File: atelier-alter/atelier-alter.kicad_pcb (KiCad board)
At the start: 2 copper layers, 81.8 x 80.2 mm, 59 parts, among them SW1 RESET, SW2 SW_DPST, SW3 SW_DPST, SW4 SW_DPST, U1 ATmega32U4-A, U2 PRTR5V0U2X, Y1 16Mhz

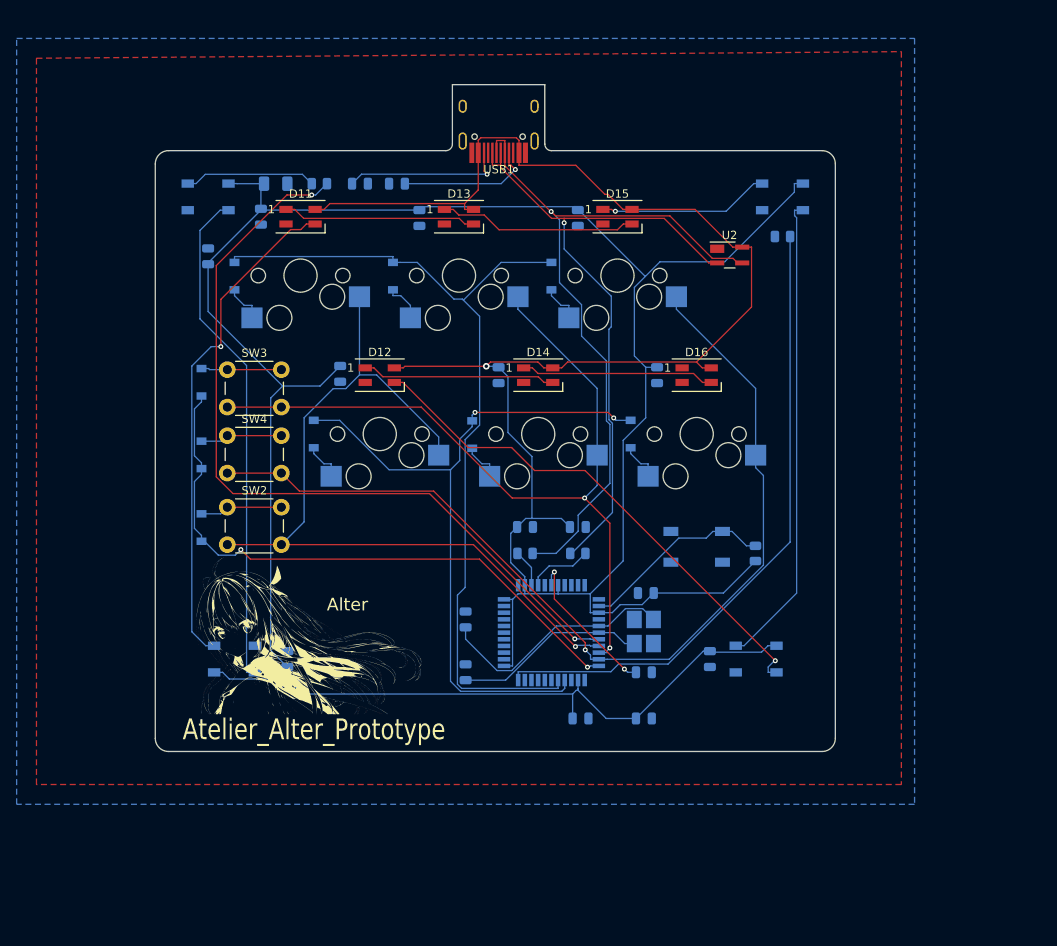
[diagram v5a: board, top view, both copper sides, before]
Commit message: update footprint, route lai mach, giam manh so luong vias
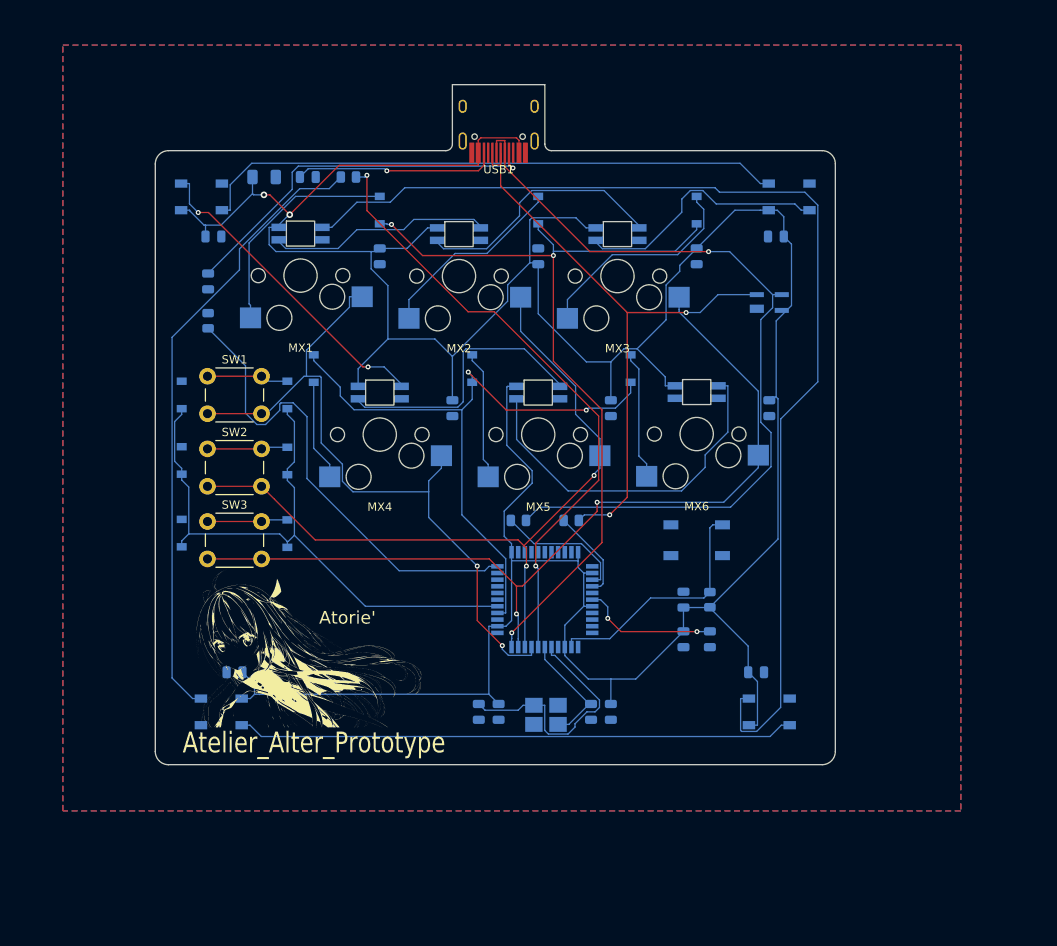
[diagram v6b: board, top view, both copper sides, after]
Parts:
- removed D1, D3, D4, D6: SOD-123, Diode_SMD:D_SOD-123
- removed D10, D7, D8: SK6812, LED_SMD:LED_SK6812_PLCC4_5.0x5.0mm_P3.2mm
- removed D14, D15, D16: SK6812MINI, LED_SMD:LED_SK6812MINI_PLCC4_3.5x3.5mm_P1.75mm
- added D21: SOD-123, Diode_SMD:D_SOD-123, B.Cu at (128.6, 84.9)
- added D22: SOD-123, Diode_SMD:D_SOD-123, B.Cu at (147.6, 84.9)
- added D23: SOD-123, Diode_SMD:D_SOD-123, B.Cu at (166.7, 84.9)
- added D31: SOD-123, Diode_SMD:D_SOD-123, B.Cu at (125.4, 88.1)
- added D32: SOD-123, Diode_SMD:D_SOD-123, B.Cu at (125.4, 96.0)
- added D33: SOD-123, Diode_SMD:D_SOD-123, B.Cu at (125.4, 104.8)
- added DT11: SK6812, LED_SMD:LED_SK6812_PLCC4_5.0x5.0mm_P3.2mm, B.Cu at (115.1, 64.3)
- C14, C17: value 100uF -> 100nF
- C2: value 1uF -> 22pF
- C4: value 22pF -> 0.1uF
- C6: value 0.1uF -> 1uF
- C8, C9: value 100nF -> 100uF
- D11, D12, D13: value SK6812MINI -> SOD-123; footprint LED_SMD:LED_SK6812MINI_PLCC4_3.5x3.5mm_P1.75mm -> Diode_SMD:D_SOD-123; moved to B.Cu
- D2, D5: value SOD-123 -> SK6812; footprint Diode_SMD:D_SOD-123 -> LED_SMD:LED_SK6812_PLCC4_5.0x5.0mm_P3.2mm
- MX1, MX2, MX3, MX4, MX5, MX6: value MX-NoLED -> Cherry_MX_Cherry_MX_RGB; footprint MX_Only:MXOnly-1U-Hotswap -> Cherry MX:Cherry-MX_PCB-Mounted_LTST-A683CEGBW_Kailh_Socket
- R4: value 10k -> 5.1k; footprint Resistor_SMD:R_0805_2012Metric -> Capacitor_SMD:C_0805_2012Metric
- R5: value 300 -> 5.1k; footprint Resistor_SMD:R_0805_2012Metric -> Capacitor_SMD:C_0805_2012Metric
- R6: value 5.1k -> 10k; footprint Capacitor_SMD:C_0805_2012Metric -> Resistor_SMD:R_0805_2012Metric
- R7: value 5.1k -> 300; footprint Capacitor_SMD:C_0805_2012Metric -> Resistor_SMD:R_0805_2012Metric
- SW1: value RESET -> SW_DPST; footprint random-keyboard-parts:SKQG-1155865 -> Button_Switch_THT:SW_PUSH_6mm_H9.5mm; moved to F.Cu
- SW4: value SW_DPST -> RESET; footprint Button_Switch_THT:SW_PUSH_6mm_H9.5mm -> random-keyboard-parts:SKQG-1155865; moved to B.Cu
- U2: moved to B.Cu
- moved R4 69.3 mm to (115.9, 74.5), turned to 90 degrees
- moved SW1 62.3 mm to (115.8, 85.9), turned to 0 degrees
- moved D5 58.6 mm to (183.4, 126.2), turned to 0 degrees
- moved SW4 57.8 mm to (174.6, 105.6), turned to 180 degrees
- moved C17 55.9 mm to (116.5, 69.1), turned to 0 degrees
- moved C9 49.7 mm to (136.5, 71.4)
- moved C10 49.5 mm to (119.1, 121.4), turned to 180 degrees
- moved C12 48.0 mm to (164.3, 89.7)
- moved C14 42.9 mm to (184.2, 69.1), turned to 180 degrees
- moved D2 35.2 mm to (117.5, 126.2), turned to 180 degrees
- moved C8 34.6 mm to (145.3, 89.7)
- moved C15 32.8 mm to (183.4, 89.7)
- moved D13 28.6 mm to (174.6, 65.9), turned to 90 degrees
- moved R6 28.1 mm to (115.9, 79.2), turned to 90 degrees
- moved C13 27.7 mm to (155.6, 71.4), turned to -90 degrees
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- renumbered Alter to Atorie'
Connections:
- C14 pad 1: GND -> +5V
- C14 pad 2: +5V -> GND
- C17 pad 1: GND -> +5V
- C17 pad 2: +5V -> GND
- C4 pad 1: GND -> +5V
- C4 pad 2: Net-(C4-Pad2) -> GND
- C6 pad 1: +5V -> GND
- C6 pad 2: GND -> Net-(C6-Pad2)
- C8 pad 1: +5V -> GND
- C8 pad 2: GND -> +5V
- C9 pad 1: +5V -> GND
- C9 pad 2: GND -> +5V
- D11 pad 1: Net-(D11-Pad1) -> ROW1
- D11 pad 2: GND -> Net-(D11-Pad2)
- D12 pad 1: Net-(D12-Pad1) -> ROW1
- D12 pad 2: GND -> Net-(D12-Pad2)
- D13 pad 1: Net-(D13-Pad1) -> ROW1
- D13 pad 2: GND -> Net-(D13-Pad2)
- D2 pad 1: ROW2 -> GND
- D5 pad 1: ROW1 -> GND
- D5 pad 2: Net-(D5-Pad2) -> Net-(D2-Pad4)
- MX1 pad 1: COL1 -> GND
- MX1 pad 2: Net-(D1-Pad2) -> D11
- MX2 pad 1: COL1 -> GND
- MX2 pad 2: Net-(D2-Pad2) -> Net-(MX1-Pad3)
- MX3 pad 1: COL2 -> GND
- MX3 pad 2: Net-(D3-Pad2) -> Net-(MX2-Pad3)
- MX4 pad 1: COL2 -> GND
- MX4 pad 2: Net-(D4-Pad2) -> D21
- MX5 pad 1: COL3 -> GND
- MX5 pad 2: Net-(D5-Pad2) -> Net-(MX4-Pad3)
- MX6 pad 1: COL3 -> GND
- MX6 pad 2: Net-(D6-Pad2) -> Net-(MX5-Pad3)
- R4 pad 1: Net-(R4-Pad1) -> GND
- R4 pad 2: GND -> Net-(R4-Pad2)
- R5 pad 1: RGB -> GND
- R5 pad 2: Net-(D7-Pad2) -> Net-(R5-Pad2)
- R6 pad 1: GND -> Net-(R6-Pad1)
- R6 pad 2: Net-(R6-Pad2) -> GND
- R7 pad 1: GND -> RGB
- R7 pad 2: Net-(R7-Pad2) -> Net-(D2-Pad2)
- SW1 pad 1: GND -> Net-(D31-Pad2)
- SW1 pad 2: Net-(R3-Pad1) -> COL1
- SW2 pad 1: Net-(D17-Pad2) -> Net-(D32-Pad2)
- SW2 pad 2: COL1 -> COL2
- SW3 pad 1: Net-(D18-Pad2) -> Net-(D33-Pad2)
- SW3 pad 2: COL2 -> COL3
- SW4 pad 1: Net-(D19-Pad2) -> GND
- SW4 pad 2: COL3 -> Net-(R3-Pad1)
- U1 pad 16: Net-(C4-Pad2) -> Net-(C3-Pad2)
- U1 pad 17: Net-(C3-Pad2) -> Net-(C2-Pad2)
- U1 pad 22: ROW3 -> ROW1
- U1 pad 27: ROW1 -> ROW3
- U1 pad 33: Net-(R4-Pad1) -> Net-(R6-Pad1)
- U1 pad 6: Net-(C2-Pad2) -> Net-(C6-Pad2)
- USB1 pad 10: Net-(R7-Pad2) -> Net-(R5-Pad2)
- USB1 pad 4: Net-(R6-Pad2) -> Net-(R4-Pad2)
- Y1 pad 1: Net-(C4-Pad2) -> Net-(C3-Pad2)
- Y1 pad 3: Net-(C3-Pad2) -> Net-(C2-Pad2)
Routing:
- net +5V: track 482.4 -> 403.9 mm, vias 1 -> 2
- net Net-(R4-Pad1): track 76.9 -> 0.00 mm
- net D11: track 60.5 -> 135.6 mm, vias 1 -> 0
- net Net-(D2-Pad2): track 4.81 -> 75.2 mm
- net Net-(D2-Pad4): track 0.00 -> 67.0 mm
- net Net-(D7-Pad4): track 60.9 -> 0.00 mm
- net Net-(R6-Pad1): track 0.00 -> 57.4 mm
- net Net-(R4-Pad2): track 0.00 -> 45.4 mm, vias 0 -> 1
- net Net-(MX5-Pad3): track 0.00 -> 43.4 mm
- net Net-(MX4-Pad3): track 0.00 -> 33.3 mm
- net Net-(MX2-Pad3): track 0.00 -> 30.7 mm
- net Net-(C4-Pad2): track 29.2 -> 0.00 mm
- net Net-(D11-Pad2): track 0.00 -> 27.1 mm
- net Net-(MX1-Pad3): track 0.00 -> 26.8 mm
- net Net-(D13-Pad2): track 0.00 -> 26.4 mm
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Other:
- board size 81.8 x 80.2 mm -> 81.8 x 81.8 mm

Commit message: add M2 mounting hole
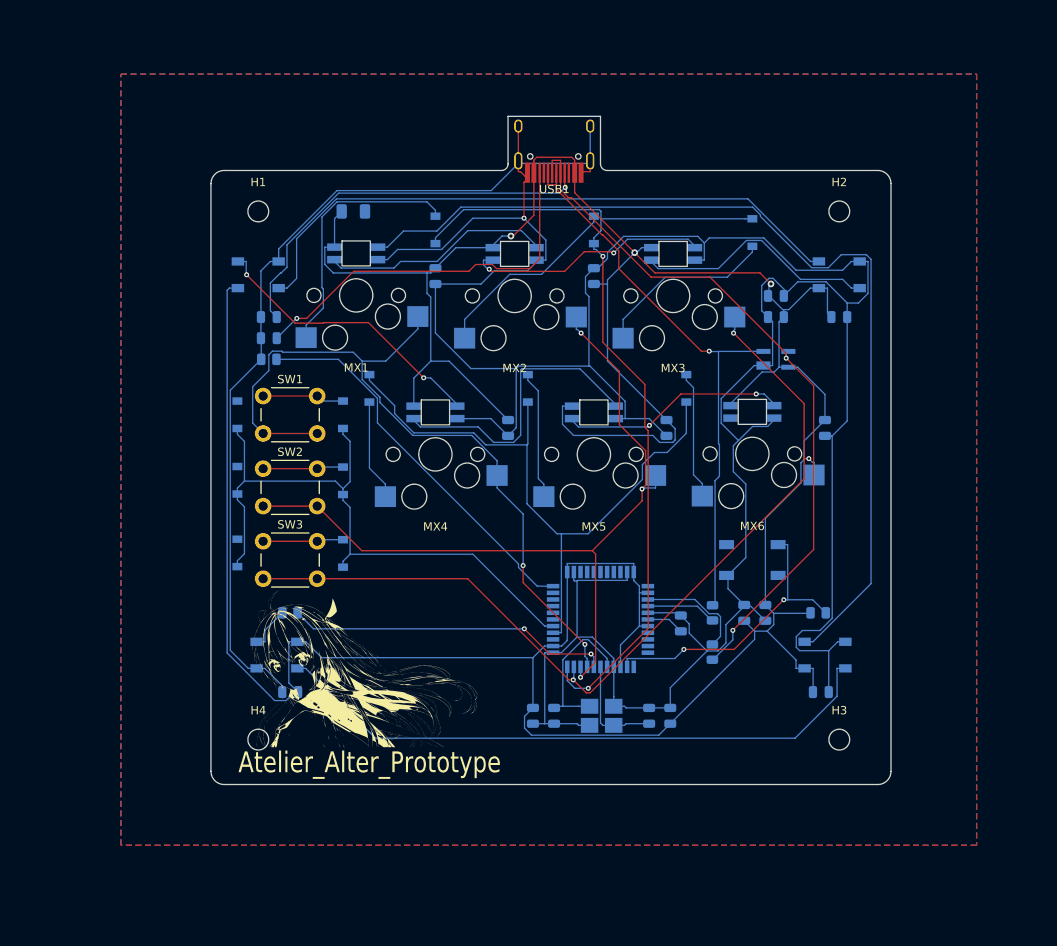
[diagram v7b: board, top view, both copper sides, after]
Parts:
- added H1: MountingHole, MountingHole:MountingHole_2.5mm, F.Cu at (121.9, 66.0)
- added H2: MountingHole, MountingHole:MountingHole_2.5mm, F.Cu at (191.8, 66.0)
- added H3: MountingHole, MountingHole:MountingHole_2.5mm, F.Cu at (191.8, 129.5)
- added H4: MountingHole, MountingHole:MountingHole_2.5mm, F.Cu at (121.9, 129.5)
- moved C17 75.9 mm to (191.8, 78.7)
- moved R7 52.9 mm to (125.7, 114.3)
- moved R1 28.2 mm to (176.5, 119.0), turned to 90 degrees
- moved C1 20.6 mm to (171.4, 126.7), turned to 90 degrees
- moved R2 20.3 mm to (176.5, 114.3), turned to -90 degrees
- moved R5 19.9 mm to (123.2, 81.3), turned to 0 degrees
- moved R3 13.1 mm to (189.2, 114.3), turned to 180 degrees
- moved DT11 11.6 mm to (121.9, 73.7)
- moved F1 11.5 mm to (133.3, 66.0)
- moved D9 11.1 mm to (191.8, 73.7)
- moved C16 10.6 mm to (184.2, 76.2), turned to 180 degrees
- moved C5 9.97 mm to (182.9, 114.3), turned to -90 degrees
- moved C14 9.68 mm to (184.2, 78.7)
- moved D2 9.56 mm to (124.2, 119.4)
- moved D5 9.56 mm to (190.0, 119.4)
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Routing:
- net GND: track 0.00 -> 485.0 mm, vias 0 -> 1
- net Net-(D2-Pad2): track 75.2 -> 5.35 mm
- net RGB: track 74.8 -> 39.0 mm
- net Net-(R5-Pad2): track 24.4 -> 46.4 mm
- net D11: track 135.6 -> 115.2 mm
- net Net-(MX5-Pad3): track 43.4 -> 27.2 mm, vias 0 -> 2
- net +5V: track 403.9 -> 418.9 mm, vias 2 -> 3
- net D-: track 99.2 -> 85.5 mm, vias 1 -> 2
- net Net-(C6-Pad2): track 16.6 -> 4.55 mm, vias 2 -> 0
- net Net-(C3-Pad2): track 29.7 -> 18.2 mm
- net Net-(R6-Pad1): track 57.4 -> 46.5 mm
- net ROW1: track 100.0 -> 108.4 mm, vias 3 -> 2
- net Net-(D2-Pad4): track 67.0 -> 74.8 mm
- net Net-(R3-Pad1): track 29.4 -> 36.2 mm, vias 0 -> 2
- net COL2: track 91.0 -> 96.7 mm, vias 2 -> 3
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- added copper zone on B.Cu, net +5V
- added copper zone on F.Cu, net +5V
- removed copper zone on B.Cu, net GND
- removed copper zone on F.Cu, net GND
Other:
- board size 81.8 x 81.8 mm -> 81.8 x 80.3 mm

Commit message: rework mot chut
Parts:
- removed F1: 500mA, Fuse:Fuse_1206_3216Metric
- C12, C13, C15, C16, C8, C9: value 100uF -> 100nF
- R4, R5: footprint Capacitor_SMD:C_0805_2012Metric -> Resistor_SMD:R_0805_2012Metric
- moved SW4 38.3 mm to (143.5, 114.3)
- moved D11 24.4 mm to (124.5, 83.8)
- moved D12 24.4 mm to (143.5, 83.8)
- moved D13 24.2 mm to (162.6, 83.8), turned to 90 degrees
- moved D22 19.9 mm to (162.6, 105.4), turned to 0 degrees
- moved D21 19.9 mm to (143.5, 105.4), turned to 180 degrees
- moved D23 19.7 mm to (181.2, 105.4), turned to 180 degrees
- moved C16 5.68 mm to (181.6, 71.1), turned to 90 degrees
- moved C13 2.71 mm to (162.6, 71.1), turned to 90 degrees
- moved C9 2.71 mm to (143.5, 71.1)
- moved R4 2.54 mm to (120.7, 78.7)
- moved R5 2.54 mm to (120.7, 81.3)
- moved R6 2.54 mm to (120.7, 83.8)
- moved H2 1.27 mm to (193.0, 66.0)
- moved H3 1.27 mm to (193.0, 129.5)
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- renumbered DT11 to D14
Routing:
- net GND: track 485.0 -> 411.3 mm, vias 1 -> 0
- net +5V: track 418.9 -> 378.2 mm, vias 3 -> 2
- net ROW2: track 79.0 -> 50.6 mm
- net Net-(D11-Pad2): track 31.0 -> 3.71 mm
- net D11: track 115.2 -> 87.9 mm, vias 0 -> 2
- net ROW1: track 108.4 -> 83.1 mm
- net Net-(D12-Pad2): track 23.3 -> 3.64 mm
- net Net-(D13-Pad2): track 21.8 -> 3.64 mm
- net COL1: track 91.1 -> 107.6 mm
- net Net-(R3-Pad1): track 36.2 -> 50.0 mm, vias 2 -> 3
- net Net-(R4-Pad2): track 48.0 -> 60.5 mm
- net Net-(D23-Pad2): track 15.4 -> 7.34 mm
- net D+: track 69.6 -> 77.3 mm, vias 1 -> 2
- net Net-(C3-Pad2): track 18.2 -> 25.0 mm
- net Net-(MX4-Pad3): track 35.8 -> 29.2 mm, vias 0 -> 2
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- added copper zone on B.Cu, net GND
- added copper zone on F.Cu, net GND
- removed copper zone on B.Cu, net +5V
- removed copper zone on F.Cu, net +5V
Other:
- board size 81.8 x 80.3 mm -> 81.3 x 80 mm
